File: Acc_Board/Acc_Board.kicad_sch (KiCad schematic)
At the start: 70 parts, among them J1 AIRs Power, J10 Conn_01x02_Pin, J12 776087-1, J3 IMD BAT, J4 HV Power, J5 HVIL, J6 IMD, J7 Current Sensor, J8 Fans, J9 Shutdown IL, K1 Relay_SPST-NO, K2 Latching Relay, Q1 STS6NF20V, Q2 STS6NF20V, Q3 STS6NF20V, Q4 STS6NF20V, U1 ISO1050DUB, U12 LM555N, U15 MCP6004, U17 NAND, U2 NUCLEO-L432KC, U4 PQDE6W-Q110-S5-H-D, U5 R-78B5.0-2.0, U8 LM7809_TO220

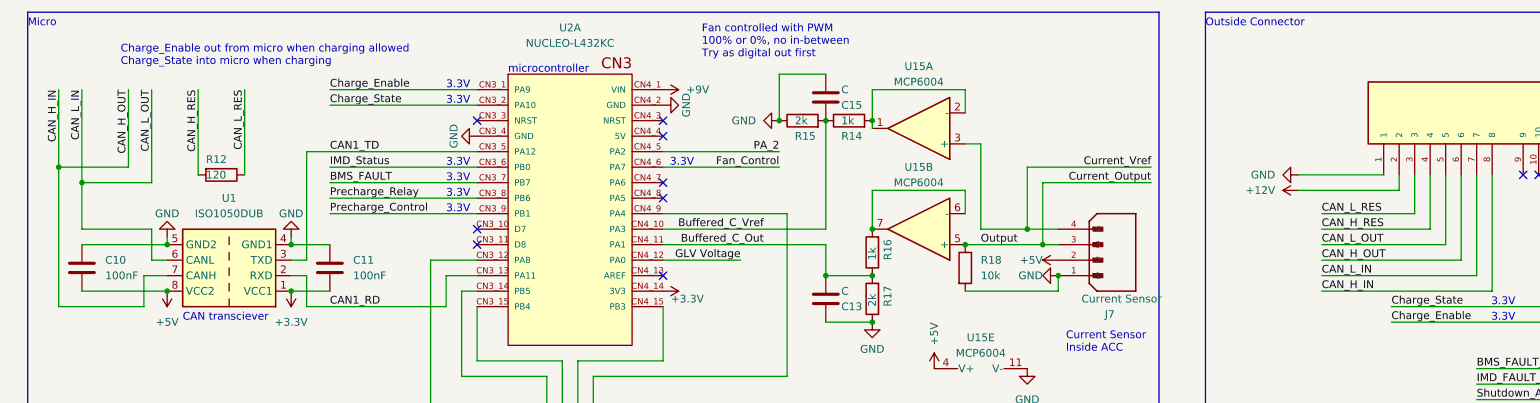
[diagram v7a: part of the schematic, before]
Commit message: More ACC board CAN changes
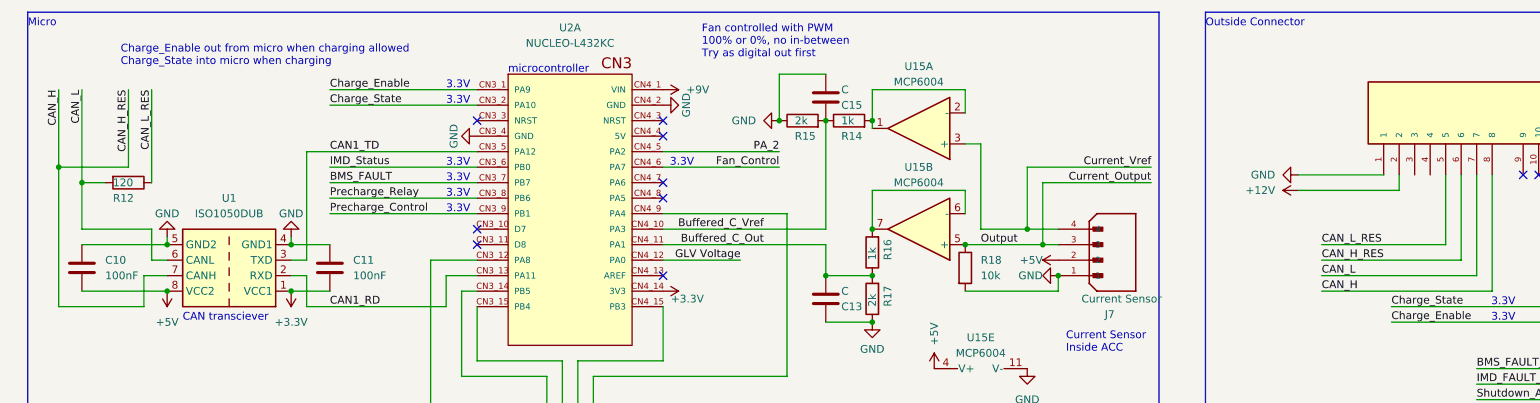
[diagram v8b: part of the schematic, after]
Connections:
- net CAN_L_RES: now also J12.5; no longer J12.3
- net CAN_H_IN renamed CAN_H
- net CAN_H_RES: no longer names the net of J12.4
- net CAN_H_RES: no longer R12.2
- net CAN_L_IN renamed CAN_L
- net CAN_L: now also R12.2; no longer J12.5
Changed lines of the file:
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@@
     (stroke (width 0) (type default))
   )
-  (wire (pts (xy 43.18 27.94) (xy 43.18 43.18))
-    (stroke (width 0) (type default))
-  )
   (wire (pts (xy 168.91 189.23) (xy 170.18 189.23))
     (stroke (width 0) (type default))
@@
     (stroke (width 0) (type default))
   )
-  (wire (pts (xy 252.73 41.91) (xy 252.73 50.8))
-    (stroke (width 0) (type default))
-  )
   (wire (pts (xy 168.91 189.23) (xy 168.91 198.12))
     (stroke (width 0) (type default))
@@
     (stroke (width 0) (type default))
   )
-  (wire (pts (xy 234.95 50.8) (xy 252.73 50.8))
-    (stroke (width 0) (type default))
-  )
   (wire (pts (xy 374.65 153.67) (xy 370.84 153.67))
     (stroke (width 0) (type default))
@@
     (stroke (width 0) (type default))
   )
+  (wire (pts (xy 31.75 43.18) (xy 35.56 43.18))
+    (stroke (width 0) (type default))
+  )
   (wire (pts (xy 176.53 125.73) (xy 176.53 142.24))
     (stroke (width 0) (type default))
@@
     (stroke (width 0) (type default))
   )
-  (wire (pts (xy 39.37 27.94) (xy 39.37 40.64))
-    (stroke (width 0) (type default))
-  )
   (wire (pts (xy 176.53 189.23) (xy 175.26 189.23))
     (stroke (width 0) (type default))
@@
     (stroke (width 0) (type default))
   )
-  (wire (pts (xy 50.8 27.94) (xy 50.8 41.91))
+  (wire (pts (xy 39.37 27.94) (xy 39.37 40.64))
     (stroke (width 0) (type default))
   )
@@
     (stroke (width 0) (type default))
   )
-  (wire (pts (xy 43.18 43.18) (xy 31.75 43.18))
-    (stroke (width 0) (type default))
-  )
   (wire (pts (xy 127 38.1) (xy 146.05 38.1))
     (stroke (width 0) (type default))
@@
     (stroke (width 0) (type default))
   )
-  (wire (pts (xy 58.42 27.94) (xy 58.42 41.91))
+  (wire (pts (xy 43.18 27.94) (xy 43.18 43.18))
     (stroke (width 0) (type default))
   )
@@
     (stroke (width 0) (type default))
   )
-  (wire (pts (xy 250.19 41.91) (xy 250.19 48.26))
-    (stroke (width 0) (type default))
-  )
   (wire (pts (xy 275.59 41.91) (xy 275.59 66.04))
     (stroke (width 0) (type default))
   )
-  (wire (pts (xy 39.37 40.64) (xy 27.94 40.64))
+  (wire (pts (xy 27.94 40.64) (xy 39.37 40.64))
     (stroke (width 0) (type default))
   )
@@
     (stroke (width 0) (type default))
   )
-  (wire (pts (xy 234.95 48.26) (xy 250.19 48.26))
-    (stroke (width 0) (type default))
-  )
   (wire (pts (xy 186.69 40.64) (xy 207.01 40.64))
     (stroke (width 0) (type default))
@@
     (effects (font (size 1.27 1.27)) (justify left bottom))
   )
-  (label "CAN_H_RES" (at 50.8 27.94 270) (fields_autoplaced)
+  (label "CAN_H_RES" (at 39.37 27.94 270) (fields_autoplaced)
     (effects (font (size 1.27 1.27)) (justify right bottom))
   )
@@
     (effects (font (size 1.27 1.27)) (justify left bottom))
   )
-  (label "CAN_H_RES" (at 234.95 50.8 0) (fields_autoplaced)
-    (effects (font (size 1.27 1.27)) (justify left bottom))
-  )
   (label "Buffered_C_Vref" (at 143.51 50.8 180) (fields_autoplaced)
     (effects (font (size 1.27 1.27)) (justify right bottom))
@@
     (effects (font (size 1.27 1.27)) (justify left bottom))
   )
-  (label "CAN_L_OUT" (at 234.95 53.34 0) (fields_autoplaced)
+  (label "CAN_L_RES" (at 234.95 53.34 0) (fields_autoplaced)
     (effects (font (size 1.27 1.27)) (justify left bottom))
   )
@@
     (effects (font (size 1.27 1.27)) (justify right bottom))
   )
-  (label "CAN_H_IN" (at 27.94 27.94 270) (fields_autoplaced)
+  (label "CAN_H" (at 27.94 27.94 270) (fields_autoplaced)
     (effects (font (size 1.27 1.27)) (justify right bottom))
   )
@@
     (effects (font (size 1.27 1.27)) (justify right bottom))
   )
-  (label "CAN_H_IN" (at 234.95 60.96 0) (fields_autoplaced)
+  (label "CAN_H" (at 234.95 60.96 0) (fields_autoplaced)
     (effects (font (size 1.27 1.27)) (justify left bottom))
   )
@@
     (effects (font (size 1.27 1.27)) (justify left bottom))
   )
-  (label "CAN_L_RES" (at 234.95 48.26 0) (fields_autoplaced)
-    (effects (font (size 1.27 1.27)) (justify left bottom))
-  )
   (label "BMS_FAULT_5V" (at 264.16 144.78 0) (fields_autoplaced)
     (effects (font (size 1.27 1.27)) (justify left bottom))
@@
     (effects (font (size 1.27 1.27)) (justify left bottom))
   )
-  (label "CAN_H_OUT" (at 234.95 55.88 0) (fields_autoplaced)
+  (label "CAN_H_RES" (at 234.95 55.88 0) (fields_autoplaced)
     (effects (font (size 1.27 1.27)) (justify left bottom))
   )
-  (label "CAN_H_OUT" (at 39.37 27.94 270) (fields_autoplaced)
-    (effects (font (size 1.27 1.27)) (justify right bottom))
-  )
   (label "TS+" (at 166.37 125.73 270) (fields_autoplaced)
     (effects (font (size 1.27 1.27)) (justify right bottom))
@@
     (effects (font (size 1.27 1.27)) (justify left bottom))
   )
-  (label "CAN_L_IN" (at 234.95 58.42 0) (fields_autoplaced)
+  (label "CAN_L" (at 234.95 58.42 0) (fields_autoplaced)
     (effects (font (size 1.27 1.27)) (justify left bottom))
   )
@@
     (effects (font (size 1.27 1.27)) (justify left bottom))
   )
-  (label "CAN_L_IN" (at 31.75 27.94 270) (fields_autoplaced)
+  (label "CAN_L" (at 31.75 27.94 270) (fields_autoplaced)
     (effects (font (size 1.27 1.27)) (justify right bottom))
   )
@@
     (effects (font (size 1.27 1.27)) (justify right bottom))
   )
-  (label "CAN_L_OUT" (at 43.18 27.94 270) (fields_autoplaced)
-    (effects (font (size 1.27 1.27)) (justify right bottom))
-  )
-  (label "CAN_L_RES" (at 58.42 27.94 270) (fields_autoplaced)
+  (label "CAN_L_RES" (at 43.18 27.94 270) (fields_autoplaced)
     (effects (font (size 1.27 1.27)) (justify right bottom))
   )
@@
     )
   )
-  (symbol (lib_name "R_3") (lib_id "Device:R") (at 54.61 41.91 270) (unit 1)
-    (in_bom yes) (on_board yes) (dnp no)
-    (property "Reference" "R12" (at 52.07 39.37 90)
-      (effects (font (size 1.27 1.27)) (justify left))
-    )
-    (property "Value" "120" (at 52.07 41.91 90)
-      (effects (font (size 1.27 1.27)) (justify left))
-    )
-    (property "Footprint" "Resistor_SMD:R_0805_2012Metric_Pad1.20x1.40mm_HandSolder" (at 54.61 40.132 90)
-      (effects (font (size 1.27 1.27)) hide)
-    )
-    (property "Datasheet" "~" (at 54.61 41.91 0)
-      (effects (font (size 1.27 1.27)) hide)
-    )
-    (pin "1")
-    (pin "2")
-    (instances
-      (project "Acc_Board"
-        (path "/e19d26dd-723b-45e6-9d59-b1730158e759"
-          (reference "R12") (unit 1)
-        )
-      )
-    )
-  )
   (symbol (lib_name "R_2") (lib_id "Device:R") (at 233.68 154.94 180) (unit 1)
     (in_bom yes) (on_board yes) (dnp no)
@@
         )
       )
+    )
+  )
+  (symbol (lib_name "R_3") (lib_id "Device:R") (at 39.37 43.18 270) (unit 1)
+    (in_bom yes) (on_board yes) (dnp no)
+    (property "Reference" "R12" (at 36.83 45.72 90)
+      (effects (font (size 1.27 1.27)) (justify left))
+    )
+    (property "Value" "120" (at 36.83 43.18 90)
+      (effects (font (size 1.27 1.27)) (justify left))
+    )
+    (property "Footprint" "Resistor_SMD:R_0805_2012Metric_Pad1.20x1.40mm_HandSolder" (at 39.37 41.402 90)
+      (effects (font (size 1.27 1.27)) hide)
+    )
+    (property "Datasheet" "~" (at 39.37 43.18 0)
+      (effects (font (size 1.27 1.27)) hide)
+    )
+    (pin "1")
+    (pin "2")
+    (instances
+      (project "Acc_Board"
+        (path "/e19d26dd-723b-45e6-9d59-b1730158e759"
+          (reference "R12") (unit 1)
+        )
+      )
